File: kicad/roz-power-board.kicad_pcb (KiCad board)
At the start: 2 copper layers, 80 x 42 mm, 87 parts, among them CON1 USB-MICRO-B, J1 Jumper_Switch, J2 Jumper_Switch, J3 Jumper_Switch, J4 Jumper_Switch, J5 Jumper_Switch, J6 Jumper_Switch, J7 Jumper_Switch, J8 Jumper_Switch, P1 Wall, P10 GPIO_A5, P11 GPIO_A6, P12 GPIO_A7, P13 BIOLOID_BUS_1, P14 GPIO_B8, P15 GPIO_B9, P16 BIOLOID_BUS_2, P17 BIOLOID_BUS_3, P18 BIOLOID_BUS_4, P19 BIOLOID_BUS_5, P2 Battery, P20 BIOLOID_BUS_6, P21 rPi Power, P23 UART_BOOT, P25 BATT_BACKUP, P26 BUS, P3 BATT_BALANCE, P4 ALT_3.3_IN, P5 UART_1, P6 I2C_2, P7 SPI_2, P8 5V Regulator, P9 GPIO_A4, Q1 BS-170, Q2 STD30PF03LT4, Q3 STD30PF03LT4, SW1 Bus Power, SW2 PowerButton, SW3 RESET_SW, SW4 BOOT_SW, U1 LM3480-3.3, U2 LTC4412, U3 STM32F401xD_UFQFPN48, X1 32.768kHz, X2 8MHz

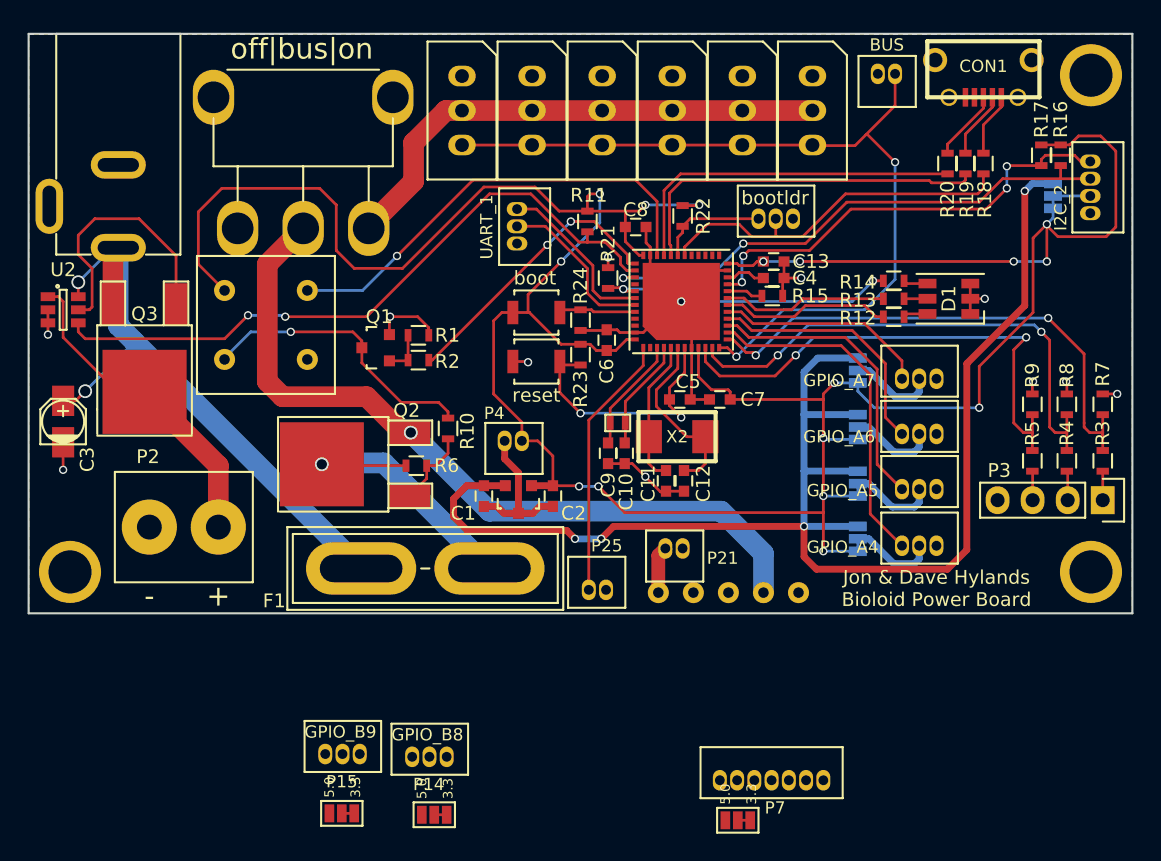
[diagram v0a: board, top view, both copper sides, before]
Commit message: more fixes to power board pcb
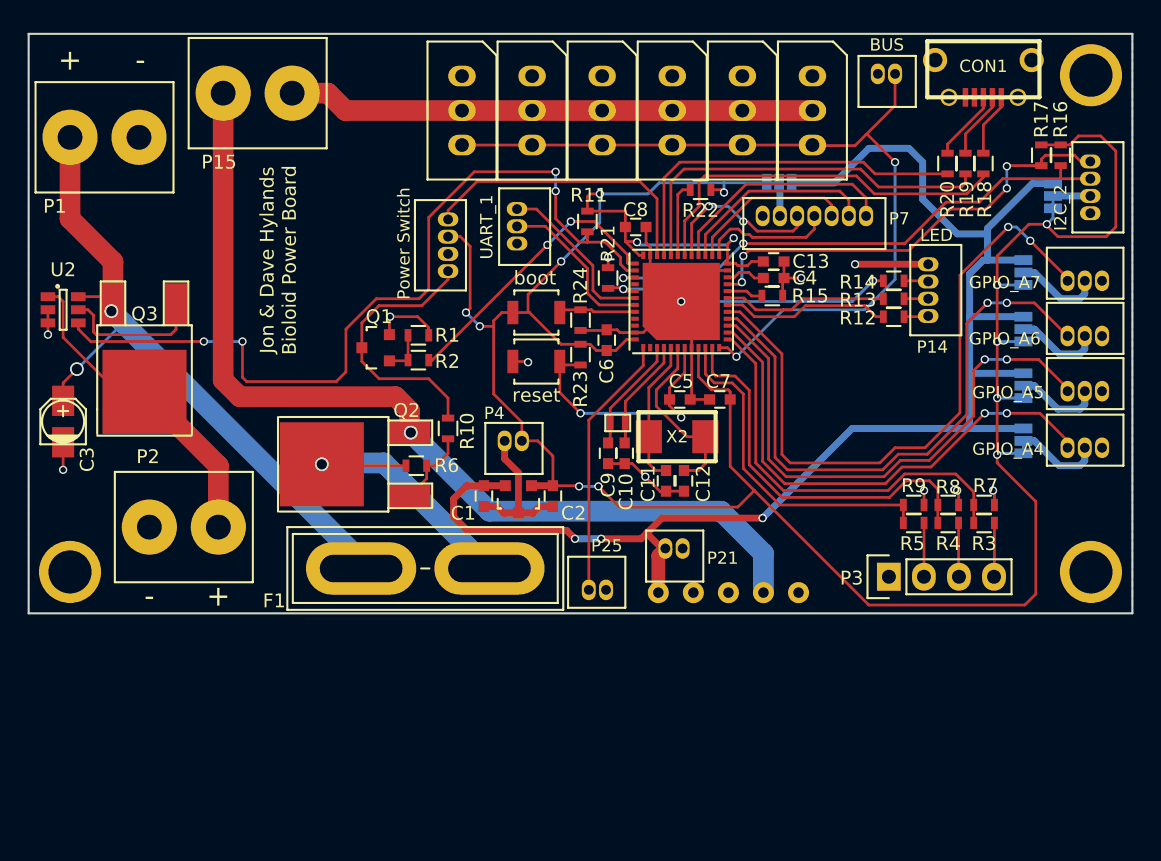
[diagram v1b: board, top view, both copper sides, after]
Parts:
- removed D1: LED_RGB, LEDs:LED_RGB_PLLC-6
- removed J7, J8: Jumper_Switch, MicroPython-Parts-new:Jumper-Switch
- removed P23: UART_BOOT, MicroPython-Parts-new:SIL_3_050
- removed SW1: Bus Power, MicroPython-Parts-new:RA-Switch-5Amp
- removed SW2: PowerButton, MicroPython-Parts-new:DPST_Mom_Switch
- added Power Switch: PowerButton, MicroPython-Parts-new:SIL_4_050, F.Cu at (130.4, 117.2)
- J2: moved to B.Cu
- P1: footprint MicroPython-Parts-new:PowerJack -> MicroPython-Parts-new:TerminalBlock
- P14: value GPIO_B8 -> LED; footprint MicroPython-Parts-new:SIL_3_050 -> MicroPython-Parts-new:SIL_4_050
- P15: value GPIO_B9 -> Bus Switch; footprint MicroPython-Parts-new:SIL_3_050 -> MicroPython-Parts-new:TerminalBlock
- moved P14 51.7 mm to (165.2, 116.7), turned to 270 degrees
- moved P15 48.1 mm to (116.6, 104.3), turned to 180 degrees
- moved J2 46.3 mm to (154.4, 110.8), turned to 180 degrees
- moved P7 42.3 mm to (160.7, 113.2), turned to 180 degrees
- moved P3 16.5 mm to (162.3, 139.3), turned to 0 degrees
- moved J6 13.9 mm to (172.1, 117.3)
- moved J3 13.9 mm to (172.1, 129.5)
- moved J4 13.9 mm to (172.1, 125.5)
- moved J5 13.9 mm to (172.1, 121.4)
- moved P10 13.9 mm to (175.3, 125.9)
- moved P11 13.9 mm to (175.3, 121.9)
- moved P12 13.9 mm to (175.3, 117.9)
- moved P9 13.9 mm to (175.3, 130.0)
- moved R7 11.3 mm to (169.2, 134.2), turned to 180 degrees
- moved R8 11.3 mm to (166.7, 134.2), turned to 180 degrees
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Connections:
- P14 pad 1: GPIO_B8 -> GND
- P14 pad 2: Net-(J7-Pad2) -> Net-(P14-Pad2)
- P14 pad 3: GND -> Net-(P14-Pad3)
- P15 pad 1: GPIO_B9 -> +SW_12V
- P15 pad 2: Net-(J8-Pad2) -> +12V
- P3 pad 1: Net-(P3-Pad1) -> GND
- P3 pad 4: GND -> Net-(P3-Pad4)
- R12 pad 2: Net-(D1-Pad6) -> Net-(P14-Pad4)
- R13 pad 2: Net-(D1-Pad5) -> Net-(P14-Pad3)
- R14 pad 2: Net-(D1-Pad4) -> Net-(P14-Pad2)
- R3 pad 2: Net-(P3-Pad1) -> Net-(P3-Pad4)
- R4 pad 2: Net-(P3-Pad2) -> Net-(P3-Pad3)
- R5 pad 2: Net-(P3-Pad3) -> Net-(P3-Pad2)
- U3 pad 2: SPI_CS_2 -> Net-(U3-Pad2)
- U3 pad 29: Net-(U3-Pad29) -> SPI_CS_2
- U3 pad 45: GPIO_B8 -> Net-(U3-Pad45)
- U3 pad 46: GPIO_B9 -> Net-(U3-Pad46)
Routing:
- net GPIO_A7: track 15.4 -> 48.1 mm, vias 0 -> 2
- net +3V3: track 221.3 -> 192.9 mm, vias 16 -> 14
- net GPIO_A6: track 18.4 -> 43.3 mm, vias 0 -> 2
- net GPIO_A5: track 21.6 -> 40.0 mm, vias 0 -> 2
- net SPI_2_MOSI: track 0.00 -> 17.0 mm
- net SPI_2_MISO: track 0.00 -> 14.6 mm
- net +12V: track 56.4 -> 69.4 mm
- net SPI_2_SCK: track 0.00 -> 12.1 mm
- net SPI_CS_2: track 0.00 -> 12.1 mm, vias 0 -> 2
- net STAT_PIN: track 49.0 -> 61.1 mm, vias 2 -> 4
- net CELL1_VOLTAGE: track 36.7 -> 24.6 mm, vias 2 -> 0
- net SWITCH_PIN: track 33.2 -> 21.3 mm, vias 1 -> 0
- net GPIO_A4: track 25.0 -> 36.8 mm, vias 0 -> 2
- net SPI_CS_1: track 0.00 -> 9.78 mm
- net CELL2_VOLTAGE: track 37.4 -> 28.3 mm, vias 2 -> 0
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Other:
- board text removed: "bootldr"
- board text removed: "off|bus|on"

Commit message: more cleanup, changes
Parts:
- added 1PIN: P***, MicroPython-Parts-new:4_40_hole, F.Cu at (103.0, 103.0)
- added 1PIN: P***, MicroPython-Parts-new:2_56_hole, F.Cu at (159.6, 139.3)
- added C14: 680uF, Capacitors_ThroughHole:C_Radial_D8_L21_P3.8, F.Cu at (117.8, 115.1)
- P1: value Wall -> Wall Power
- P21: value rPi Power -> rPi
- P25: value BATT_BACKUP -> VBAT
- P4: value ALT_3.3_IN -> ALT_3.3
- PowerSwitch: renamed from Power Switch
- moved P1 4.20 mm to (107.0, 111.4), turned to 270 degrees
- moved P3 1.20 mm to (163.6, 139.3)
- moved R3 1.20 mm to (170.4, 135.4)
- moved R4 1.20 mm to (167.8, 135.4)
- moved R5 1.20 mm to (165.3, 135.4)
- moved R7 1.20 mm to (170.4, 134.2)
- moved R8 1.20 mm to (167.8, 134.2)
- moved R9 1.20 mm to (165.3, 134.2)
- moved P21 0.45 mm to (147.3, 136.8)
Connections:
- P21 pad 1: GND -> +5V
- P21 pad 2: +5V -> GND
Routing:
- net +POWER: track 50.3 -> 43.0 mm
- net +12V: track 69.4 -> 73.1 mm
- net CELL2_VOLTAGE: track 28.3 -> 29.5 mm
- net CELL3_VOLTAGE: track 29.9 -> 31.1 mm
- net CELL1_VOLTAGE: track 24.6 -> 25.8 mm
- net +5V: track 107.0 -> 108.1 mm
- net +3V3: track 192.9 -> 193.7 mm
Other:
- board text added: "+-"
- board text added: "Bus Switch"
- board text added: "G"
- board text added: "Jon & Dave Hylands Bioloid Power Board powered by MicroPython"
- board text added: "S"
- board text added: "V"
- board text removed: "Jon & Dave Hylands Bioloid Power Board"
